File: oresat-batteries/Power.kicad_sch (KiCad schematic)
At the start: 86 parts, among them J2 FTS-102-01-X-SJ, Q3 DMP3050LVT-7, U3 MIC842LYC5, U6 TS5A21366DCUR

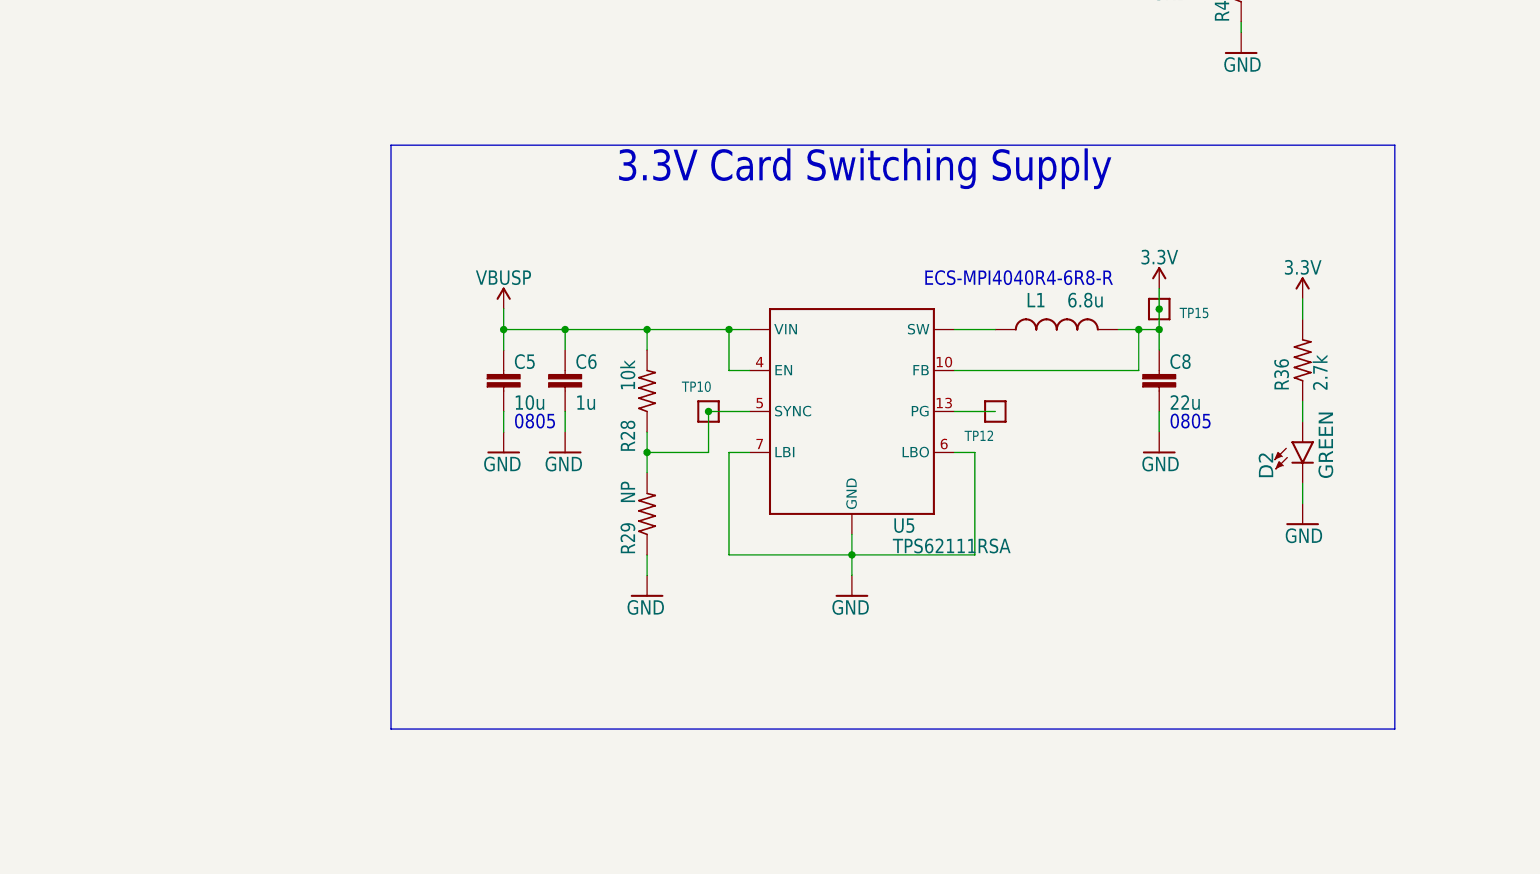
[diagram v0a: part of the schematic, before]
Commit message: 3v3 Regulator Swap
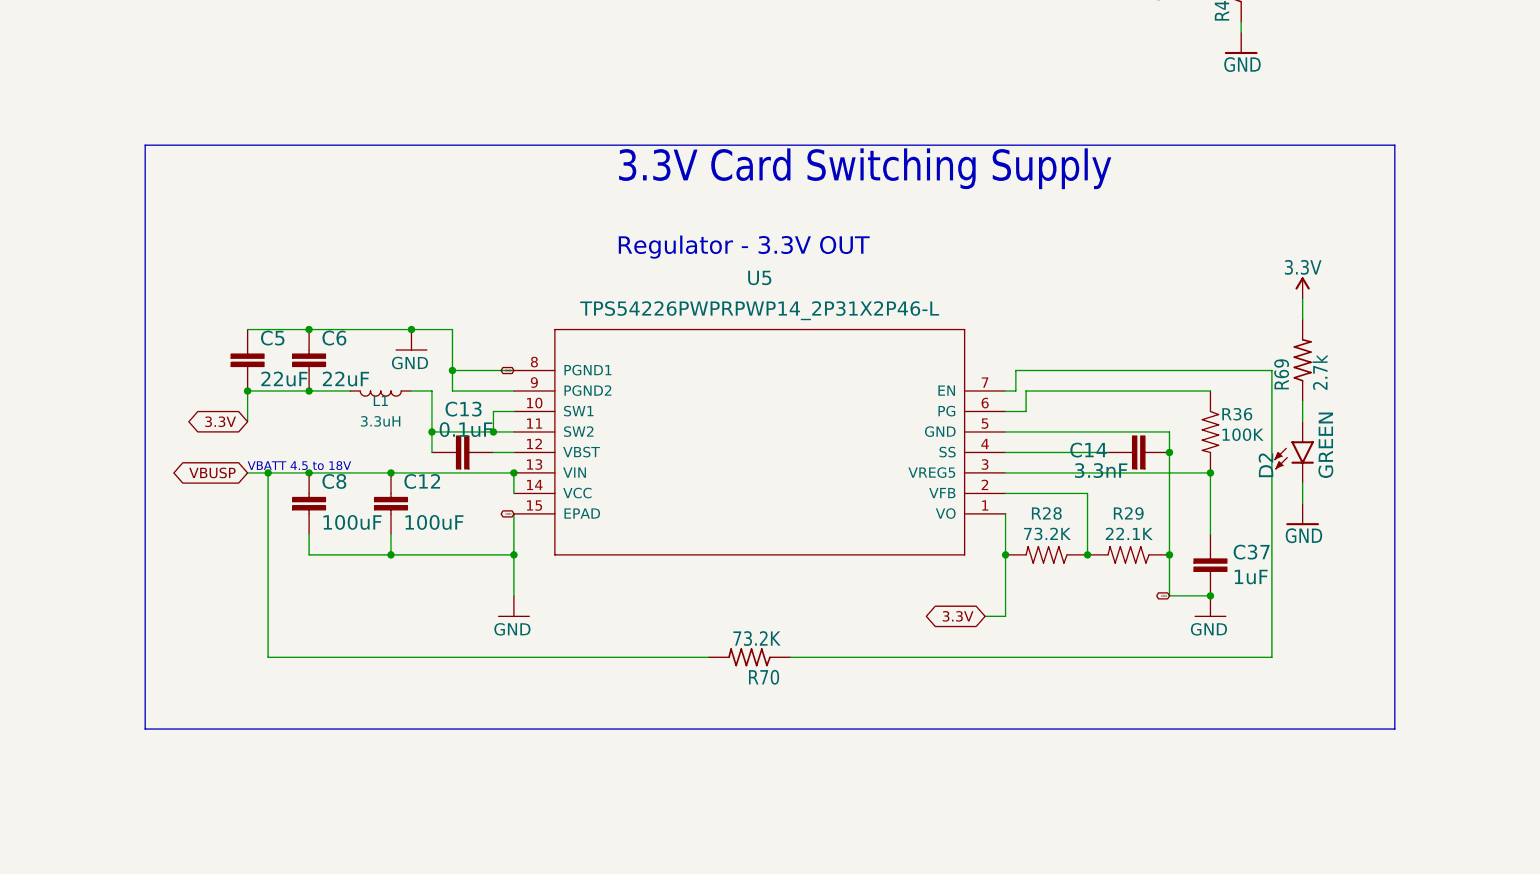
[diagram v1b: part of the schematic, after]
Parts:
- removed C5, C8: (no value), Capacitor_SMD:C_0805_2012Metric, symbol oresat-batteries-eagle-import:C-EU0805-B-NOSILK
- removed C6: (no value), oresat-footprints:0603-SMALL, symbol oresat-batteries-eagle-import:C-EU0603-C-NOSILK
- removed L1: (no value), oresat-footprints:L-ECS-MPI4040, symbol oresat-batteries-eagle-import:L-ECS-MPI4040
- removed R28, R29: (no value), oresat-footprints:0603-SMALL, symbol oresat-batteries-eagle-import:R-US_0603-C-NOSILK
- removed TP10, TP12, TP15: TEST-POINT-LARGE-SQUARE, oresat-footprints:TestPoint_Pad_1.0x1.0mm, symbol oresat-batteries-eagle-import:TEST-POINT-LARGE-SQUARE
- removed U5: (no value), oresat-footprints:U-S-PVQFN-16, symbol oresat-batteries-eagle-import:TPS6211X
- added C12, C8: 100uF, Capacitor_SMD:C_1210_3225Metric, symbol mainboard:22UF-1210-16V-20%
- added C13: 0.1uF, Capacitor_SMD:C_0603_1608Metric, symbol mainboard:1.0UF-0603-16V-10%
- added C14: 3.3nF, Capacitor_SMD:C_0603_1608Metric, symbol mainboard:3.3NF-0603-100V-10%
- added C37: 1uF, Capacitor_SMD:C_0603_1608Metric, symbol mainboard:1.0UF-0603-16V-10%
- added C5, C6: 22uF, Capacitor_SMD:C_0603_1608Metric, symbol mainboard:22UF-0805-6.3V-20%
- added L1: 3.3uH, Max:L_2141, symbol Device:L
- added R28: 73.2K, Resistor_SMD:R_0603_1608Metric, symbol mainboard:R-US_R0603
- added R29: 22.1K, Resistor_SMD:R_0603_1608Metric, symbol mainboard:R-US_R0603
- added R36: 100K, Resistor_SMD:R_0603_1608Metric, symbol mainboard:R-US_R0603
- added R70: (no value), Max:0603-RES, symbol oresat-batteries-eagle-import:R-US_0603-C-NOSILK
- added U5: TPS54226PWPRPWP14_2P31X2P46-L, symbol mainboard:TPS54226PWPRPWP14_2P31X2P46-L
- R69: renamed from R36; footprint oresat-footprints:0603-SMALL -> Max:0603-RES
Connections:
- net 3.3V: now also C5.2, C6.2, L1.2, R28.2, U5.1 (VO)
- net GND: now also C12.2, C14.2, C37.2, C5.1, C6.1, C8.2, R29.1, U5.15 (EPAD), U5.5 (GND), U5.8 (PGND1), U5.9 (PGND2)
- net VBUSP: now also C12.1, C8.1, R70.2, U5.13 (VIN), U5.14 (VCC)
- new net: R70.1, U5.7 (EN)
- new net: C37.1, R36.2, U5.3 (VREG5)
- new net: R28.1, R29.2, U5.2 (VFB)
- new net: C13.1, L1.1, U5.10 (SW1), U5.11 (SW2)
- new net: C13.2, U5.12 (VBST)
- new net: R36.1, U5.6 (PG)
- new net: C14.1, U5.4 (SS)
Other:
- note added: "Regulator - 3.3V OUT"
- note added: "VBATT 4.5 to 18V"
- note removed: "0805"
- note removed: "ECS-MPI4040R4-6R8-R"
